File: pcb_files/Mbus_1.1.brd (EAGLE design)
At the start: 98.7 x 71.1 mm, 50 parts, among them IC1 NCP1117ST50T3G, IC3 ATMEGA2560-16AU, IC4 RTC_PCF8523T, J1 F-1X18-SIP-100-32Y, J2 USB_A_SMT_FEMALE, M1 SERVO, Q2 32.768, Y1 CSTCE16M0V53-R0 16MHZ

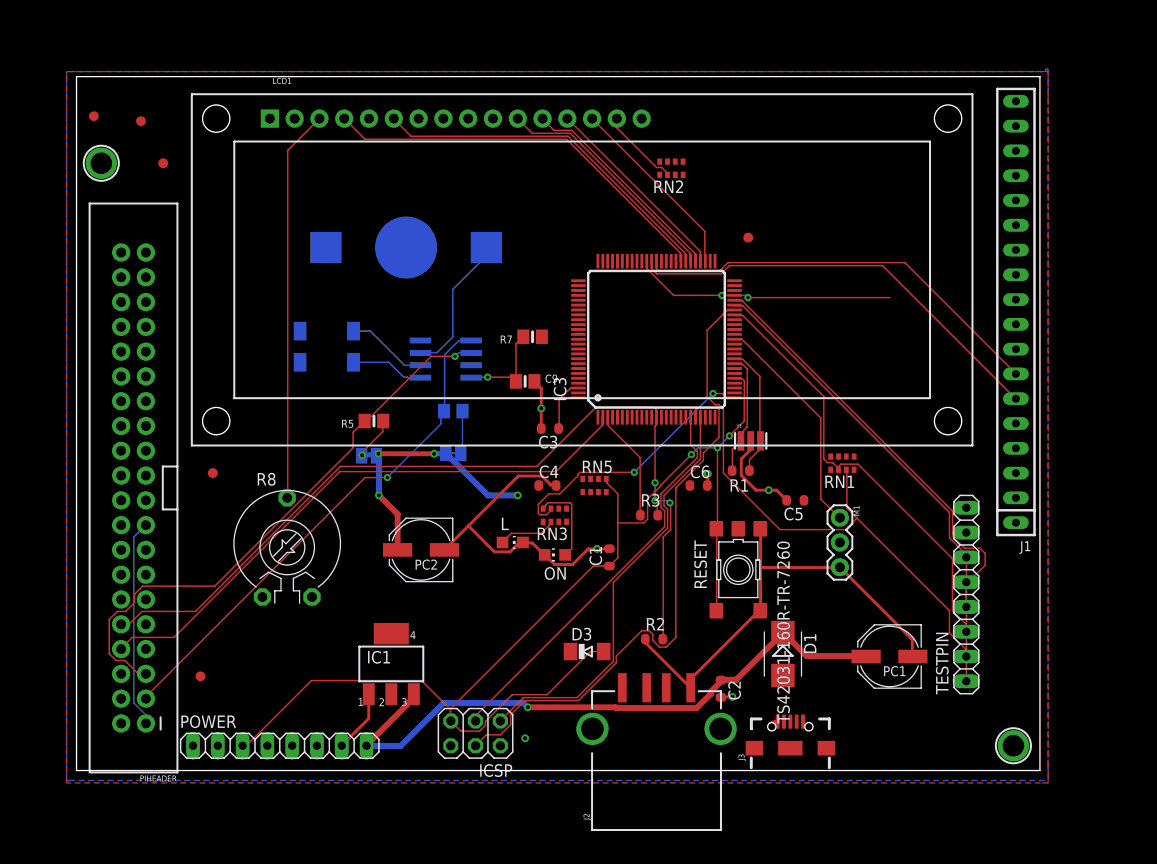
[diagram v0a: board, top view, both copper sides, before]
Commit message: A second version based on the previous one with similar layout.
Signed-off-by: Yiteng Cai <alonsochate@umich.edu>
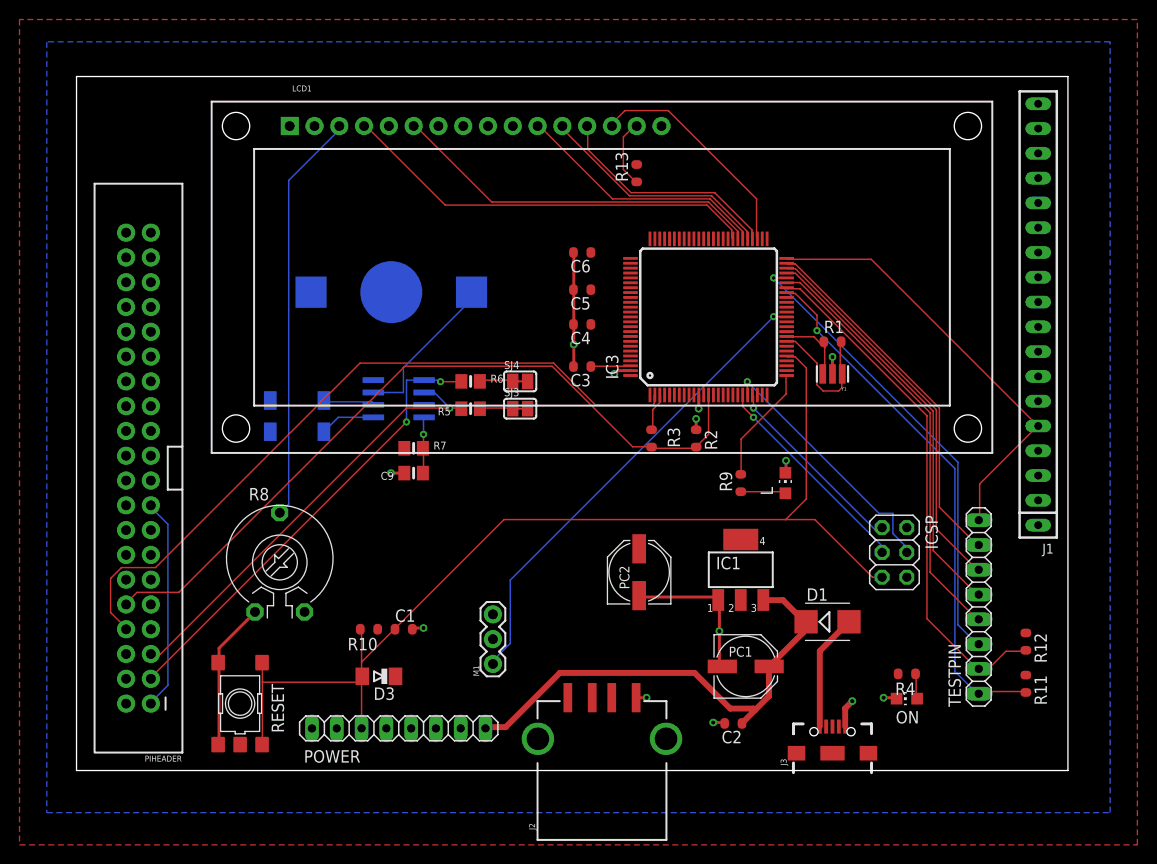
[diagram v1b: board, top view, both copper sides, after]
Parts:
- removed FD1, FD2, FD3, FD4: FIDUCIALMOUNT, SmartPrj:FIDUCIA-MOUNT
- removed FID3, FID4: FIDUCIAL"", microbuilder:FIDUCIAL_1MM
- removed RN1, RN5: 10K, resistor-dil:CAT16
- removed RN2: 220, resistor-dil:CAY16
- removed RN3: 1k, resistor-dil:CAY16
- removed U$2, U$3: MOUNTINGHOLE2.0, microbuilder:MOUNTINGHOLE_2.0_PLATED
- added R10, R11, R12: 10k, SmartPrj:R0603-ROUND
- added R13: 220, SmartPrj:R0603-ROUND
- added R4, R9: 1k, SmartPrj:R0603-ROUND
- moved RESET 52.9 mm to (16.8, 6.86), turned to 90 degrees
- moved ICSP 46.8 mm to (83.8, 22.4), turned to 270 degrees
- moved ON 39.0 mm to (85.1, 7.37)
- moved M1 38.6 mm to (42.7, 10.9), turned to 90 degrees
- moved IC1 37.1 mm to (68.1, 20.6)
- moved C5 30.7 mm to (51.8, 49.3)
- moved L 28.6 mm to (72.6, 29.5), turned to 0 degrees
- moved C6 26.7 mm to (51.8, 53.1), turned to 180 degrees
- moved PC2 22.5 mm to (57.7, 20.3), turned to 90 degrees
- moved C1 22.3 mm to (33.5, 14.5), turned to 0 degrees
- moved D3 21.5 mm to (31.0, 9.65), turned to 180 degrees
- moved R2 21.0 mm to (63.5, 34.0), turned to 270 degrees
- moved C4 16.9 mm to (51.8, 45.7), turned to 180 degrees
- moved R7 16.7 mm to (34.5, 33.0), turned to 0 degrees
- moved SJ3 16.2 mm to (45.5, 37.1), flipped to the top
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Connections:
- removed net PJ2: IC3.65
- net +5V: now also R10.1, R11.1, R12.1, R13.2, R4.2; no longer RN1.6, RN1.7, RN2.7, RN3.1, RN5.8
- net N$11: now also R13.1; no longer RN2.2
- net N$2: now also R9.1; no longer RN3.2
- net N$3: now also R4.1; no longer RN3.8
- net PB7: now also R9.2; no longer RN3.7
- net RESET: now also R10.2; no longer RN5.1
- net RXD3: no longer IC3.63
- net SCL: now also R11.2; no longer RN1.2
- net SDA: now also R12.2; no longer RN1.3
- net TXD3: no longer IC3.64
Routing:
- net PD7: track 0.00 -> 45.1 mm
- net TXD3: track 44.3 -> 0.00 mm
- net GND: track 103.1 -> 58.9 mm, vias 5 -> 13
- net RXD3: track 42.8 -> 0.00 mm
- net PD4: track 0.00 -> 41.8 mm
- net PD5: track 0.00 -> 39.7 mm
- net PD6: track 0.00 -> 37.7 mm
- net PB2: track 56.4 -> 26.5 mm, vias 0 -> 1
- net PJ2: track 26.9 -> 0.00 mm, vias 2 -> 0
- net PL3: track 23.2 -> 48.8 mm, vias 0 -> 1
- net +5V: track 24.2 -> 0.00 mm, vias 4 -> 0
- net PB3: track 43.1 -> 19.8 mm, vias 0 -> 1
- net PB1: track 41.1 -> 22.0 mm, vias 0 -> 1
- net PB7: track 27.7 -> 12.1 mm, vias 2 -> 0
- net VIN: track 65.0 -> 50.1 mm, vias 1 -> 0
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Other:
- board size 98.7 x 71.1 mm -> 101.6 x 71.1 mm
